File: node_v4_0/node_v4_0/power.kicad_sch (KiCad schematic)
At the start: 18 parts, among them Q1 2N3904, Q2 DMG1013UW, U3 ADP2108AUJ-3.3, U7 CAT3200-5

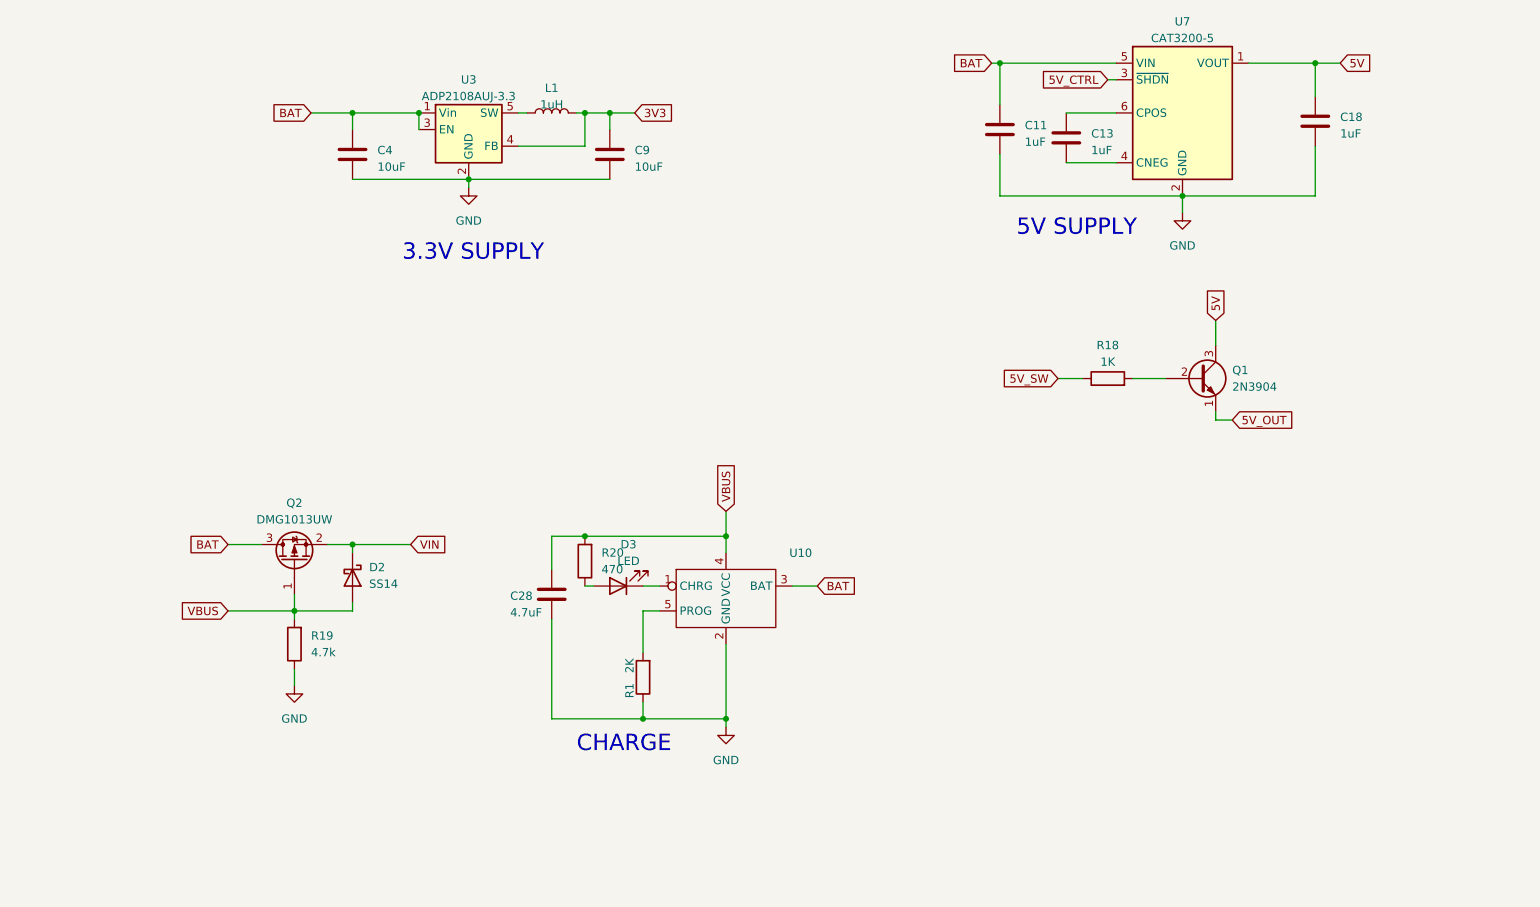
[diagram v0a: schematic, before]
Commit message: converted v4 to different format and started the schematic(from scratch again)
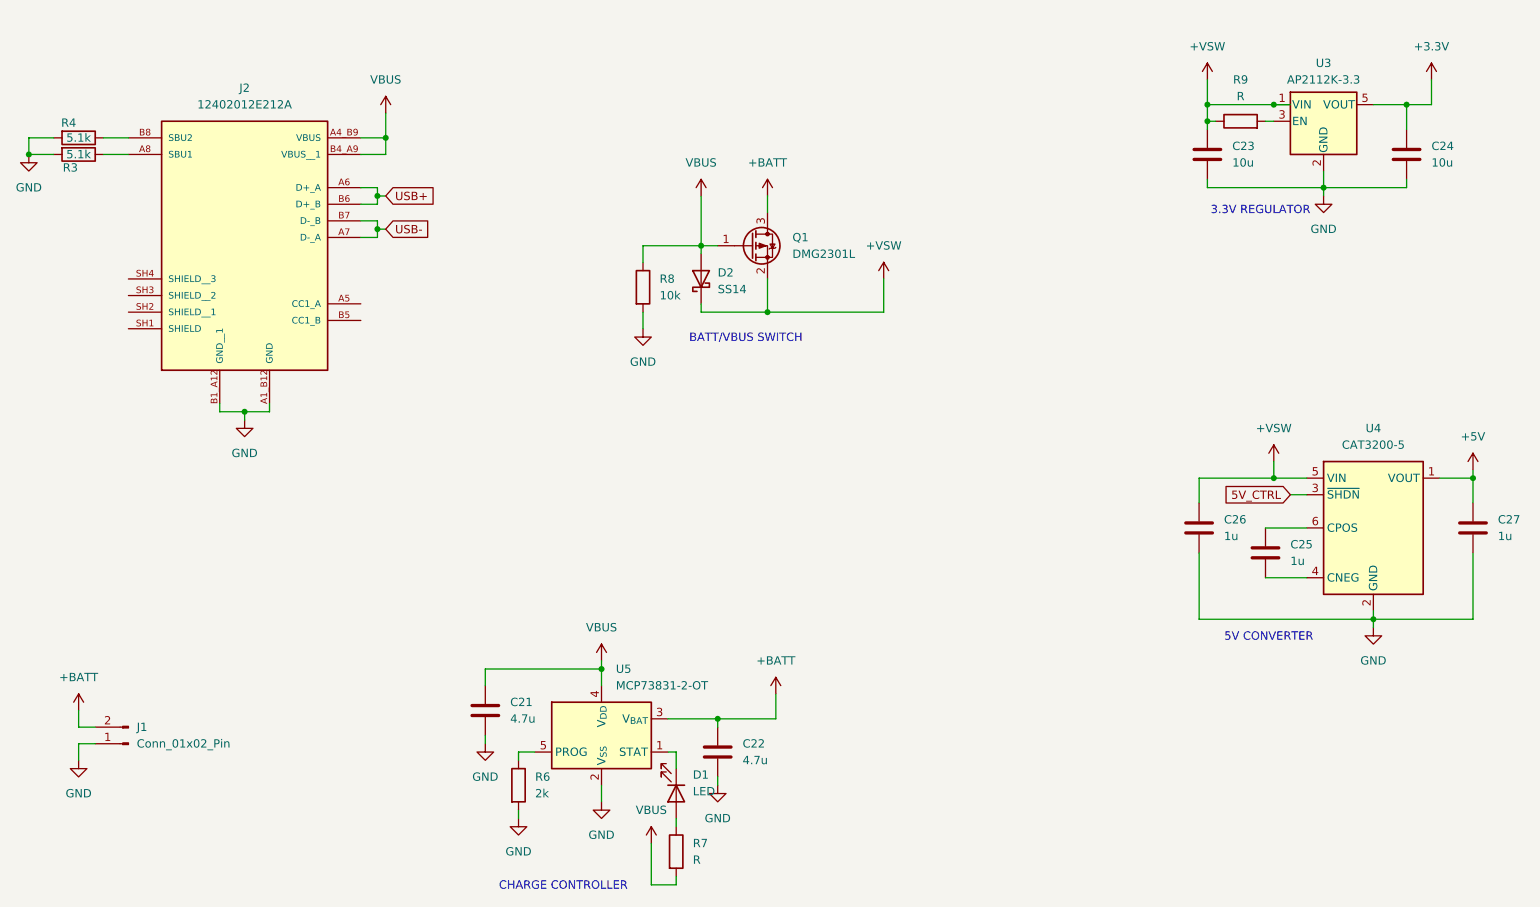
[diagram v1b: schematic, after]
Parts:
- removed C11, C13, C18: 1uF, Capacitor_SMD:C_0805_2012Metric_Pad1.18x1.45mm_HandSolder, symbol Device:C
- removed C28: 4.7uF, Capacitor_SMD:C_0805_2012Metric_Pad1.18x1.45mm_HandSolder, symbol Device:C
- removed C4, C9: 10uF, Capacitor_SMD:C_0805_2012Metric_Pad1.18x1.45mm_HandSolder, symbol Device:C
- removed D3: LED, LED_SMD:LED_1206_3216Metric_Pad1.42x1.75mm_HandSolder, symbol Device:LED
- removed L1: 1uH, Inductor_SMD:L_1008_2520Metric_Pad1.43x2.20mm_HandSolder, symbol Device:L
- removed Q1: 2N3904, Package_TO_SOT_SMD:SOT-23-3, symbol Transistor_BJT:2N3904
- removed Q2: DMG1013UW, Package_TO_SOT_SMD:SOT-23, symbol Transistor_FET:IRLML6402
- removed R1: 2K, Resistor_SMD:R_0805_2012Metric_Pad1.20x1.40mm_HandSolder, symbol Device:R
- removed R18: 1K, Resistor_SMD:R_0805_2012Metric_Pad1.20x1.40mm_HandSolder, symbol Device:R
- removed R19: 4.7k, symbol Device:R
- removed R20: 470, Resistor_SMD:R_0805_2012Metric_Pad1.20x1.40mm_HandSolder, symbol Device:R
- removed U10: ~, symbol Battery_Management:TP4054
- removed U3: ADP2108AUJ-3.3, Package_TO_SOT_SMD:TSOT-23-5, symbol Regulator_Switching:ADP2108AUJ-3.3
- removed U7: CAT3200-5, Package_TO_SOT_SMD:SOT-23-6, symbol Regulator_SwitchedCapacitor:CAT3200-5
- added C21, C22: 4.7u, Capacitor_SMD:C_0805_2012Metric_Pad1.18x1.45mm_HandSolder, symbol Device:C
- added C23, C24: 10u, Capacitor_SMD:C_0805_2012Metric_Pad1.18x1.45mm_HandSolder, symbol Device:C
- added C25, C26, C27: 1u, Capacitor_SMD:C_0805_2012Metric_Pad1.18x1.45mm_HandSolder, symbol Device:C
- added D1: LED, LED_SMD:LED_1206_3216Metric_Pad1.42x1.75mm_HandSolder, symbol Device:LED
- added J1: Conn_01x02_Pin, Connector_JST:JST_PH_B2B-PH-K_1x02_P2.00mm_Vertical, symbol Connector:Conn_01x02_Pin
- added J2: 12402012E212A, usbc:AMPHENOL_12402012E212A, symbol 12402012E212A:12402012E212A
- added Q1: DMG2301L, Package_TO_SOT_SMD:SOT-23, symbol Transistor_FET:DMG2301L
- added R3, R4: 5.1k, Resistor_SMD:R_0805_2012Metric_Pad1.20x1.40mm_HandSolder, symbol Device:R
- added R6: 2k, Resistor_SMD:R_0805_2012Metric_Pad1.20x1.40mm_HandSolder, symbol Device:R
- added R7, R9: R, Resistor_SMD:R_0805_2012Metric_Pad1.20x1.40mm_HandSolder, symbol Device:R
- added R8: 10k, Resistor_SMD:R_0805_2012Metric_Pad1.20x1.40mm_HandSolder, symbol Device:R
- added U3: AP2112K-3.3, Package_TO_SOT_SMD:SOT-23-5, symbol Regulator_Linear:AP2112K-3.3
- added U4: CAT3200-5, Package_TO_SOT_SMD:SOT-23-6, symbol Regulator_SwitchedCapacitor:CAT3200-5
- added U5: MCP73831-2-OT, Package_TO_SOT_SMD:SOT-23-5, symbol Battery_Management:MCP73831-2-OT
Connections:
- net 5V_CTRL: now also U4.3 (~{SHDN})
- net GND: now also C21.2, C22.2, C23.2, C24.2, C26.2, C27.2, J1.1 (Pin_1), J2.A1_B12 (GND), J2.B1_A12 (GND__1), R3.2, R4.2, R6.2, R8.2, U3.2 (GND), U4.2 (GND), U5.2 (V_{SS})
- net VBUS: now also C21.1, J2.A4_B9 (VBUS), J2.B4_A9 (VBUS__1), Q1.1 (G), R7.2, R8.1, U5.4 (V_{DD})
- net VIN renamed +VSW
- net +VSW: now also C23.1, C26.1, Q1.2 (S), R9.1, U3.1 (VIN), U4.5 (VIN)
- new net: R9.2, U3.3 (EN)
- new net: C25.2, U4.4 (CNEG)
- new net: C25.1, U4.6 (CPOS)
- new net: D1.1 (K), U5.1 (STAT)
- new net: D1.2 (A), R7.1
- new net: R6.1, U5.5 (PROG)
- new net: J2.B8 (SBU2), R4.1
- new net: J2.A8 (SBU1), R3.1
- new net +3.3V: C24.1, U3.5 (VOUT)
- new net +5V: C27.1, U4.1 (VOUT)
- new net +BATT: C22.1, J1.2 (Pin_2), Q1.3 (D), U5.3 (V_{BAT})
- new net USB+: J2.A6 (D+_A), J2.B6 (D+_B)
- new net USB-: J2.A7 (D-_A), J2.B7 (D-_B)
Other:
- note added: "3.3V REGULATOR"
- note added: "5V CONVERTER"
- note added: "BATT/VBUS SWITCH"
- note added: "CHARGE CONTROLLER"
- note removed: "3.3V SUPPLY"
- note removed: "5V SUPPLY"
- note removed: "CHARGE"

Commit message: more tracing, added RFM, added SIM, built power systems. converted to star ground
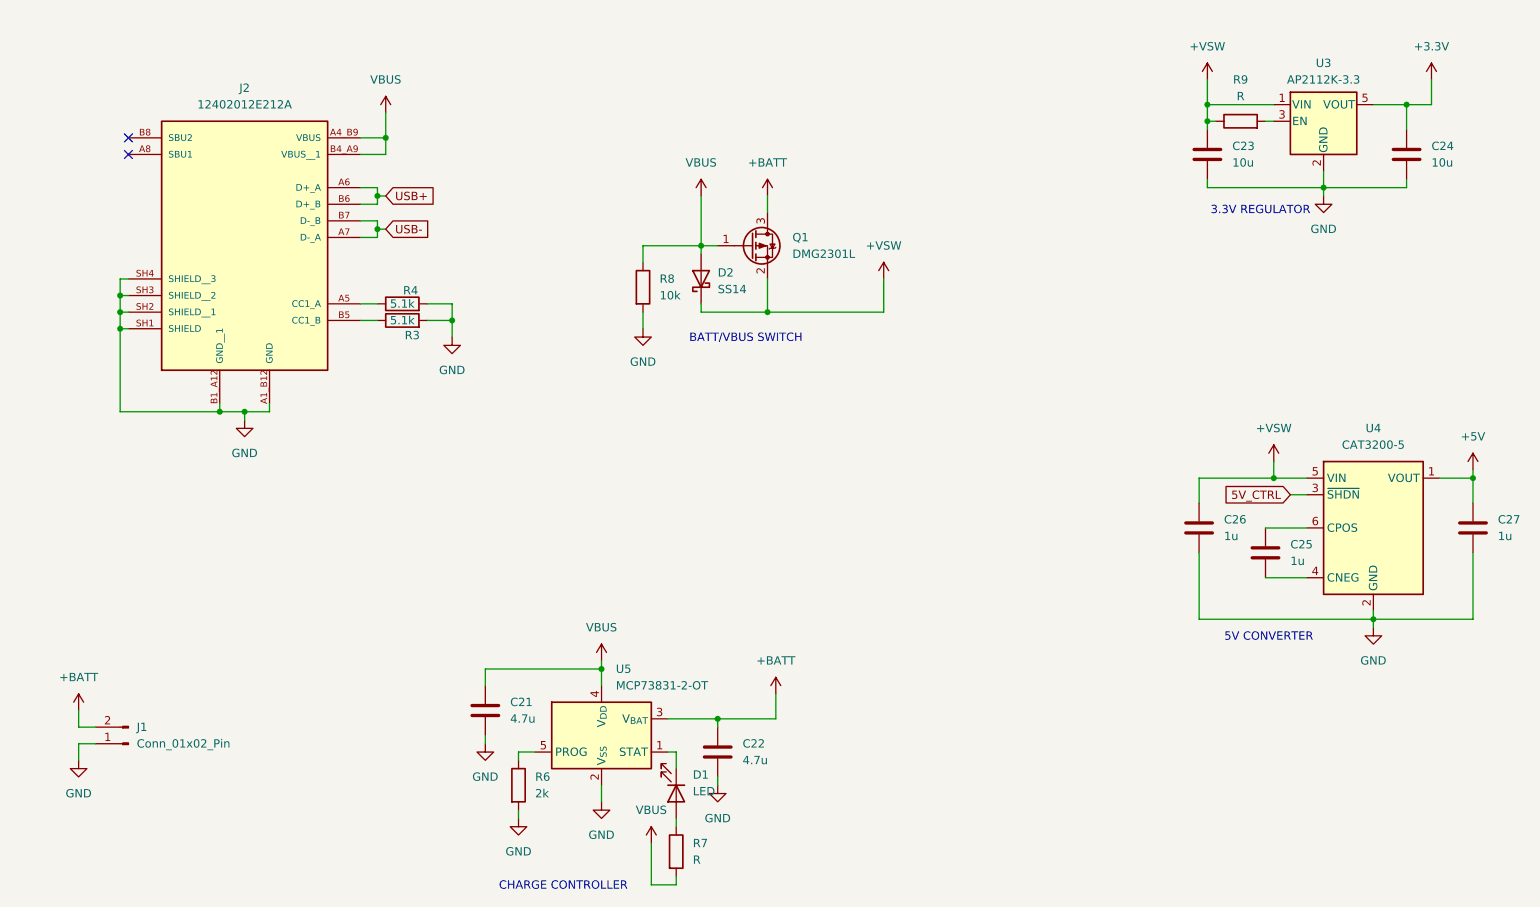
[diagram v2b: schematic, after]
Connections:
- net GND: now also J2.SH1 (SHIELD), J2.SH2 (SHIELD__1), J2.SH3 (SHIELD__2), J2.SH4 (SHIELD__3)
- net at R4.1: now also J2.A5 (CC1_A); no longer J2.B8 (SBU2)
- net at J2.A8 (SBU1): no longer R3.1
- net at J2.B5 (CC1_B): now also R3.1
- no-connect marks 0 -> 2
